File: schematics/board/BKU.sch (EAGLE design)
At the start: 76 parts, among them Q1 8MHz, Q2 32,768KHz, U1 STM32F405RGT6

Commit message: Пытаем плату БКУ компоновкой
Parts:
- removed JP1: (no value), pinhead:PINHD-1X4
- removed LED-G#2: (no value), led:LEDCHIPLED_0603
- removed R10, R11, R14, R4: 10k, resistor:R-US_R0603
- removed R19: 1M, resistor:R-US_R0603
- removed R20: 510k, resistor:R-US_R0603
- removed R28: 2k, resistor:R-US_R0603
- removed U$9: FS8205A+, CanCubeSat:FS8205A+
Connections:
- removed net 3V3: U$4.3V3/BUS
- removed net B1_KVCC: R10.1, R11.1, R19.1, R20.1, U$18.Q0
- removed net BUS-: LED-G#2.A, R20.2, U$9.S1
- removed net GND2: R27.2
- removed net N$1: JP1.4, U1.PA6/SPI1_MISO
- removed net N$10: JP1.3, U1.PA7/SPI1_MOSI
- removed net N$11: R14.1, U1.PA15
- removed net N$12: R4.1, U1.PB3
- removed net N$16: JP1.1, U1.PA4/USART2_CK
- removed net N$2: JP1.2, U1.PA5/SPI1_SCK
- removed net N$50: LED-B#2.A
- removed net N$52: LED-G#2.C, R28.2
- removed net N$8: R10.2, U$9.G1
- removed net N$9: R11.2, U$9.G2
- net 5V: no longer R28.1
- net BUS+: no longer R19.2
- net GND: now also R27.2; no longer U$9.HEAT, U$9.S2
- net N$3: now also LED-B#2.A
- net VDD: now also U$4.3V3/BUS; no longer R14.2, R4.2
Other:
- moved on the sheet: C1, C15, C16, C17, C5, R12

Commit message: Изменения в БКУ
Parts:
- GPS: value GPS -> GPSNEO6M; device CanCubeSat:GPS -> CanCubeSat:GPSNEO6M
- JTAG: device pinheadCS:PINHD-1X4 -> pinheadCS:PINHD-1X6
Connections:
- net GND: now also JTAG.1, U1.BOOT0, U1.PB2/BOOT1, U1.VSS
- net MTCK: now also JTAG.5; no longer JTAG.3
- net MTDI: now also JTAG.6; no longer JTAG.4
- net MTDO: now also JTAG.3; no longer JTAG.1
- net MTMS: now also JTAG.4; no longer JTAG.2
- net VDD: now also JTAG.2
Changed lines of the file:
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@@
 <part name="C10" library="rcl" library_urn="urn:adsk.eagle:library:334" deviceset="C-EU" device="C0603" package3d_urn="urn:adsk.eagle:package:23616/2" value="10pF"/>
 <part name="C11" library="rcl" library_urn="urn:adsk.eagle:library:334" deviceset="C-EU" device="C0603" package3d_urn="urn:adsk.eagle:package:23616/2" value="10pF"/>
-<part name="GPS" library="CanCubeSat" deviceset="GPS" device=""/>
+<part name="GPS" library="CanCubeSat" deviceset="GPS" device="NEO6M" value="GPSNEO6M"/>
 <part name="SUPPLY4" library="supply2" library_urn="urn:adsk.eagle:library:372" deviceset="GND" device=""/>
 <part name="RADIO" library="CanCubeSat" deviceset="RADIO" device=""/>
@@
 <part name="LED1" library="led" library_urn="urn:adsk.eagle:library:259" deviceset="LED" device="CHIPLED_0603" package3d_urn="urn:adsk.eagle:package:15822/2"/>
 <part name="R7" library="resistor" library_urn="urn:adsk.eagle:library:348" deviceset="R-US_" device="R0603" package3d_urn="urn:adsk.eagle:package:23555/3" value="10k"/>
-<part name="JTAG" library="pinheadCS" deviceset="PINHD-1X4" device=""/>
 <part name="MAG" library="pinheadCS" deviceset="PINHD-1X4" device=""/>
 <part name="R15" library="resistor" library_urn="urn:adsk.eagle:library:348" deviceset="R-US_" device="R0603" package3d_urn="urn:adsk.eagle:package:23555/3" value="2k"/>
@@
 <part name="LED-B#2" library="led" library_urn="urn:adsk.eagle:library:259" deviceset="LED" device="CHIPLED_0603" package3d_urn="urn:adsk.eagle:package:15822/2"/>
 <part name="R29" library="resistor" library_urn="urn:adsk.eagle:library:348" deviceset="R-US_" device="R0603" package3d_urn="urn:adsk.eagle:package:23555/3" value="10k"/>
+<part name="JTAG" library="pinheadCS" deviceset="PINHD-1X6" device=""/>
 </parts>
 <sheets>
@@
 <attribute name="VALUE" x="224.282" y="166.37" size="1.778" layer="96" rot="R90"/>
 </instance>
-<instance part="JTAG" gate="A" x="48.26" y="114.3" smashed="yes" rot="R180">
-<attribute name="NAME" x="54.61" y="106.045" size="1.778" layer="95" rot="R180"/>
-<attribute name="VALUE" x="54.61" y="121.92" size="1.778" layer="96" rot="R180"/>
-</instance>
 <instance part="MAG" gate="A" x="-86.36" y="63.5" smashed="yes" rot="R90">
 <attribute name="NAME" x="-94.615" y="57.15" size="1.778" layer="95" rot="R90"/>
@@
 <attribute name="NAME" x="232.41" y="280.8986" size="1.778" layer="95"/>
 <attribute name="VALUE" x="232.41" y="276.098" size="1.778" layer="96"/>
+</instance>
+<instance part="JTAG" gate="A" x="48.26" y="111.76" smashed="yes" rot="R180">
+<attribute name="NAME" x="52.07" y="100.965" size="1.778" layer="95" rot="R180"/>
+<attribute name="VALUE" x="54.61" y="119.38" size="1.778" layer="96" rot="R180"/>
 </instance>
 </instances>
@@
 <label x="248.92" y="279.4" size="1.778" layer="95" rot="R180"/>
 </segment>
+<segment>
+<pinref part="JTAG" gate="A" pin="1"/>
+<wire x1="50.8" y1="104.14" x2="66.04" y2="104.14" width="0.1524" layer="91"/>
+<label x="58.42" y="104.14" size="1.778" layer="95"/>
+</segment>
+<segment>
+<pinref part="U1" gate="G$1" pin="VSS"/>
+<wire x1="292.1" y1="73.66" x2="304.8" y2="73.66" width="0.1524" layer="91"/>
+<label x="299.72" y="73.66" size="1.778" layer="95"/>
+</segment>
+<segment>
+<pinref part="U1" gate="G$1" pin="BOOT0"/>
+<wire x1="231.14" y1="167.64" x2="231.14" y2="180.34" width="0.1524" layer="91"/>
+<label x="231.14" y="175.26" size="1.778" layer="95" rot="R90"/>
+</segment>
+<segment>
+<pinref part="U1" gate="G$1" pin="PB2/BOOT1"/>
+<wire x1="231.14" y1="111.76" x2="218.44" y2="111.76" width="0.1524" layer="91"/>
+<label x="218.44" y="111.76" size="1.778" layer="95"/>
+</segment>
 </net>
 <net name="5V" class="0">
@@
 <label x="-121.92" y="170.18" size="1.778" layer="95"/>
 <pinref part="U$4" gate="G$1" pin="3V3/BUS"/>
+</segment>
+<segment>
+<pinref part="JTAG" gate="A" pin="2"/>
+<wire x1="50.8" y1="106.68" x2="66.04" y2="106.68" width="0.1524" layer="91"/>
+<label x="58.42" y="106.68" size="1.778" layer="95"/>
 </segment>
 </net>
@@
 <net name="MTDI" class="0">
 <segment>
-<pinref part="JTAG" gate="A" pin="4"/>
 <wire x1="50.8" y1="116.84" x2="66.04" y2="116.84" width="0.1524" layer="91"/>
 <label x="58.42" y="116.84" size="1.778" layer="95"/>
+<pinref part="JTAG" gate="A" pin="6"/>
 </segment>
 <segment>
@@
 <net name="MTCK" class="0">
 <segment>
-<pinref part="JTAG" gate="A" pin="3"/>
 <wire x1="50.8" y1="114.3" x2="66.04" y2="114.3" width="0.1524" layer="91"/>
 <label x="58.42" y="114.3" size="1.778" layer="95"/>
+<pinref part="JTAG" gate="A" pin="5"/>
 </segment>
 <segment>
@@
 <net name="MTMS" class="0">
 <segment>
-<pinref part="JTAG" gate="A" pin="2"/>
 <wire x1="50.8" y1="111.76" x2="66.04" y2="111.76" width="0.1524" layer="91"/>
 <label x="58.42" y="111.76" size="1.778" layer="95"/>
+<pinref part="JTAG" gate="A" pin="4"/>
 </segment>
 <segment>
@@
 <net name="MTDO" class="0">
 <segment>
-<pinref part="JTAG" gate="A" pin="1"/>
 <wire x1="50.8" y1="109.22" x2="66.04" y2="109.22" width="0.1524" layer="91"/>
 <label x="58.42" y="109.22" size="1.778" layer="95"/>
-</segment>
-<segment>
+<pinref part="JTAG" gate="A" pin="3"/>
+</segment>
+<segment>

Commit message: Изменения в БКУ
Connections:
- net GND: now also U1.VSSA
- net VDD: now also U1.VDDA
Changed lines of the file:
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@@
 <wire x1="292.1" y1="73.66" x2="304.8" y2="73.66" width="0.1524" layer="91"/>
 <label x="299.72" y="73.66" size="1.778" layer="95"/>
+<pinref part="U1" gate="G$1" pin="VSSA"/>
+<wire x1="292.1" y1="71.12" x2="292.1" y2="73.66" width="0.1524" layer="91"/>
+<junction x="292.1" y="73.66"/>
 </segment>
 <segment>
@@
 <label x="299.72" y="175.26" size="1.778" layer="95"/>
 <pinref part="LED2" gate="G$1" pin="A"/>
-</segment>
-<segment>
+<pinref part="U1" gate="G$1" pin="VDDA"/>
+<wire x1="292.1" y1="172.72" x2="292.1" y2="175.26" width="0.1524" layer="91"/>
+<junction x="292.1" y="175.26"/>
+</segment>
+<segment>

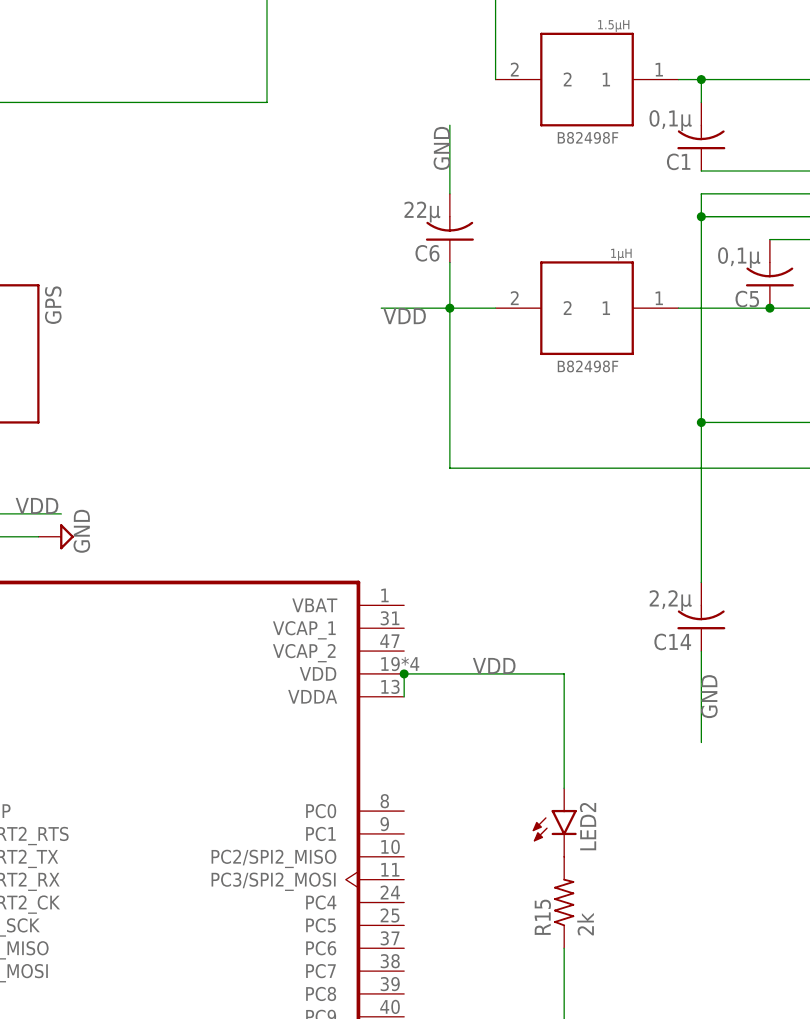
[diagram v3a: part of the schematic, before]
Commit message: Добавлена батарейка в БКУ
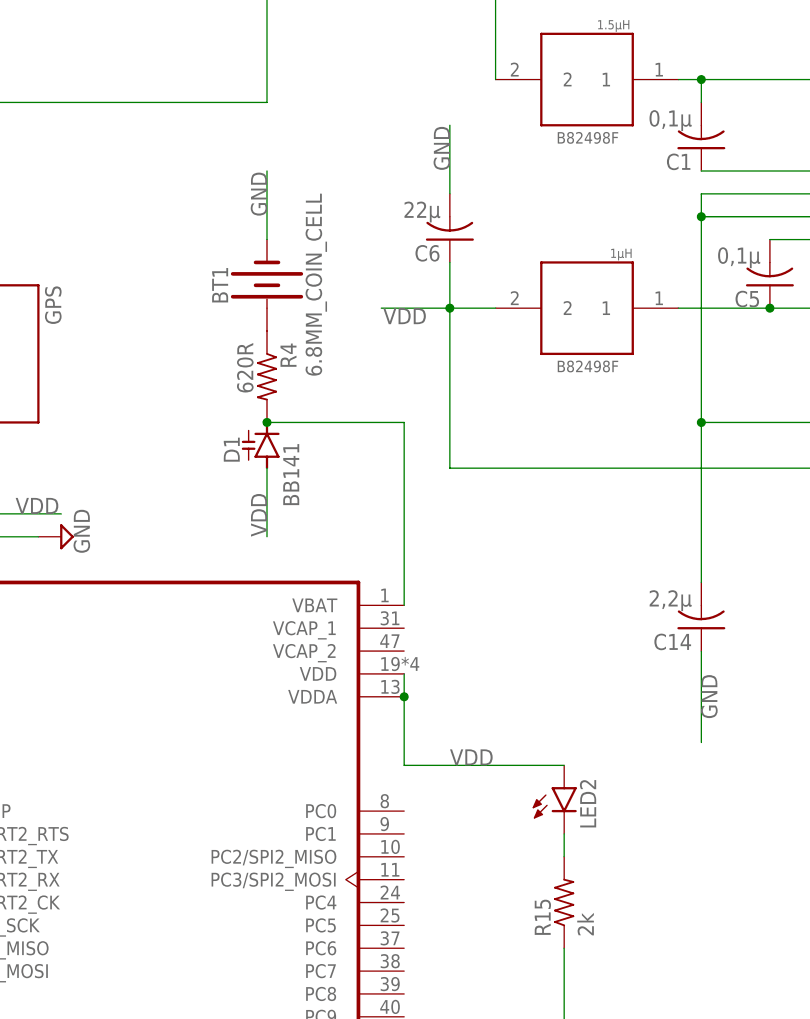
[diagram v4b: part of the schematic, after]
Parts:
- added BT1: 6.8MM_COIN_CELL, SparkFun-Batteries:BATTERY-6.8MM_SMD
- added D1: BB141, diode:BB141
- added R4: 620R, resistor:R-US_R0603
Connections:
- new net N$1: BT1.+, R4.1
- new net N$2: D1.C, R4.2, U1.VBAT
- net GND: now also BT1.-
- net VDD: now also D1.A
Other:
- moved on the sheet: LED2

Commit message: Изменения в БКУ
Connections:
- net 5V: now also RADIO.VCC
- net VDD: no longer RADIO.VCC
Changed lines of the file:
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@@
 <pinref part="BSK4" gate="A" pin="2"/>
+</segment>
+<segment>
+<pinref part="RADIO" gate="G$1" pin="VCC"/>
+<wire x1="220.98" y1="264.16" x2="220.98" y2="271.78" width="0.1524" layer="91"/>
+<label x="220.98" y="266.7" size="1.778" layer="95" rot="R90"/>
 </segment>
 </net>
@@
 </segment>
 <segment>
-<pinref part="RADIO" gate="G$1" pin="VCC"/>
-<wire x1="220.98" y1="264.16" x2="220.98" y2="271.78" width="0.1524" layer="91"/>
-<label x="220.98" y="266.7" size="1.778" layer="95" rot="R90"/>
-</segment>
-<segment>

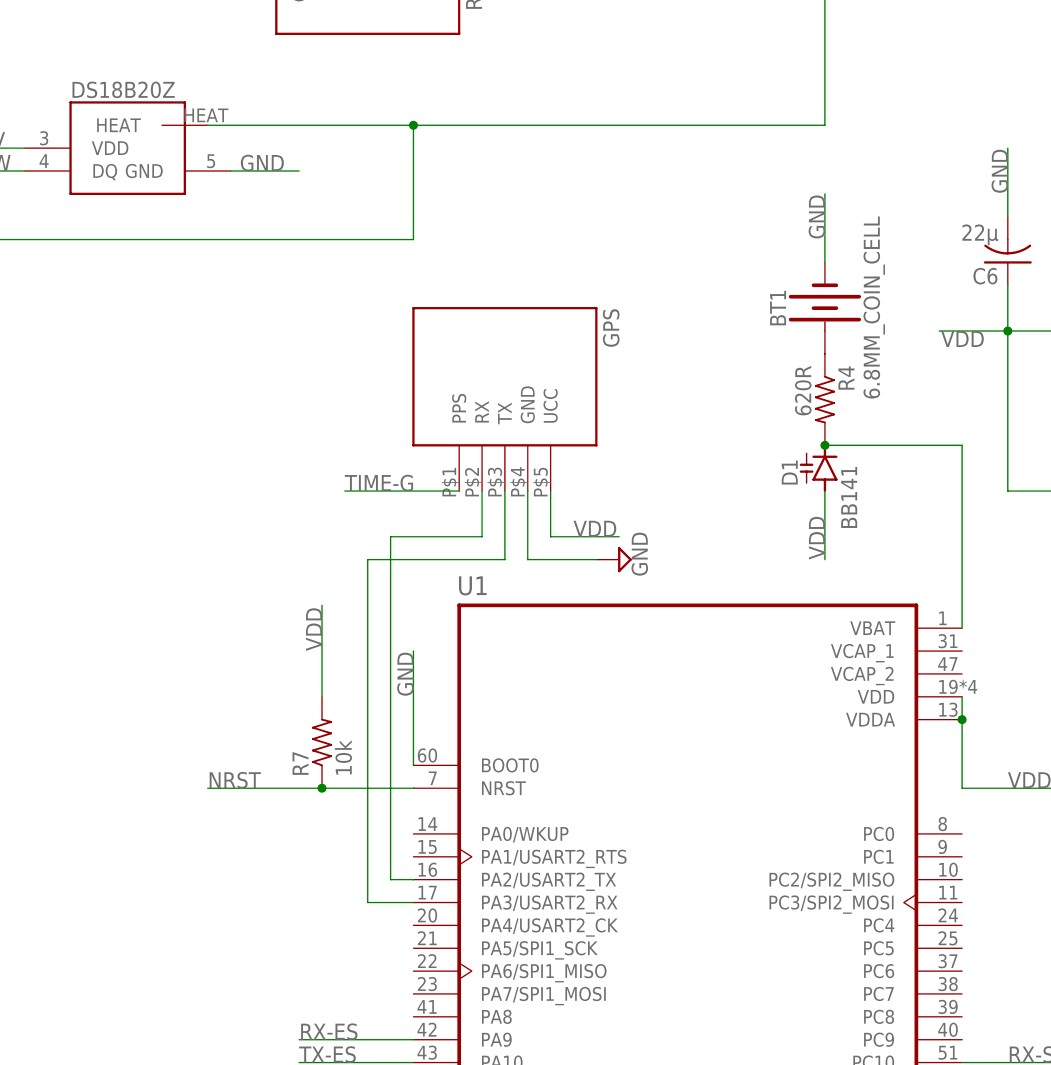
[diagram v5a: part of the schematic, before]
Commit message: Разводка БКУ кроме 1 дорожки к есп (RX-R)
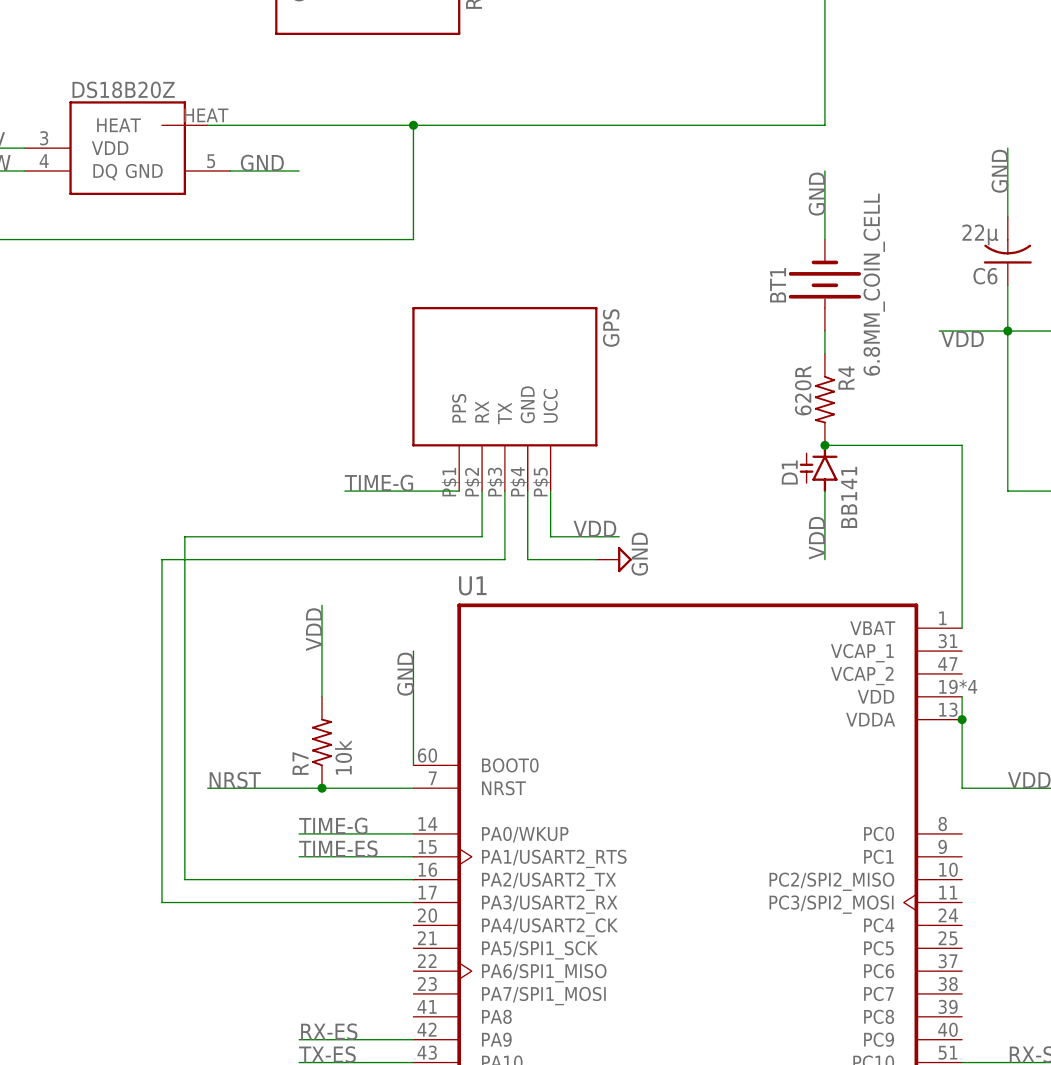
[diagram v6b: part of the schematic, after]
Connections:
- net TIME-ES: now also U1.PA1/USART2_RTS
- net TIME-G: now also U1.PA0/WKUP
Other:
- moved on the sheet: BT1
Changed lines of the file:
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@@
 <attribute name="VALUE" x="273.558" y="212.09" size="1.778" layer="96" rot="R270"/>
 </instance>
-<instance part="BT1" gate="G$1" x="276.86" y="218.44" smashed="yes" rot="R90">
-<attribute name="NAME" x="272.542" y="218.44" size="1.778" layer="95" font="vector" rot="R90" align="bottom-center"/>
-<attribute name="VALUE" x="281.178" y="218.44" size="1.778" layer="96" font="vector" rot="R90" align="top-center"/>
+<instance part="BT1" gate="G$1" x="276.86" y="220.98" smashed="yes" rot="R90">
+<attribute name="NAME" x="272.542" y="220.98" size="1.778" layer="95" font="vector" rot="R90" align="bottom-center"/>
+<attribute name="VALUE" x="281.178" y="220.98" size="1.778" layer="96" font="vector" rot="R90" align="top-center"/>
 </instance>
 </instances>
@@
 <segment>
 <pinref part="BT1" gate="G$1" pin="-"/>
-<wire x1="276.86" y1="223.52" x2="276.86" y2="231.14" width="0.1524" layer="91"/>
-<label x="276.86" y="226.06" size="1.778" layer="95" rot="R90"/>
+<wire x1="276.86" y1="226.06" x2="276.86" y2="233.68" width="0.1524" layer="91"/>
+<label x="276.86" y="228.6" size="1.778" layer="95" rot="R90"/>
 </segment>
 </net>
@@
 <segment>
 <pinref part="U1" gate="G$1" pin="PA2/USART2_TX"/>
-<wire x1="231.14" y1="154.94" x2="228.6" y2="154.94" width="0.1524" layer="91"/>
-<wire x1="228.6" y1="154.94" x2="228.6" y2="193.04" width="0.1524" layer="91"/>
+<wire x1="231.14" y1="154.94" x2="205.74" y2="154.94" width="0.1524" layer="91"/>
+<wire x1="205.74" y1="154.94" x2="205.74" y2="193.04" width="0.1524" layer="91"/>
 <pinref part="GPS" gate="G$1" pin="RX"/>
 <wire x1="238.76" y1="198.12" x2="238.76" y2="193.04" width="0.1524" layer="91"/>
-<wire x1="238.76" y1="193.04" x2="228.6" y2="193.04" width="0.1524" layer="91"/>
+<wire x1="238.76" y1="193.04" x2="205.74" y2="193.04" width="0.1524" layer="91"/>
 </segment>
 </net>
@@
 <segment>
 <pinref part="U1" gate="G$1" pin="PA3/USART2_RX"/>
-<wire x1="231.14" y1="152.4" x2="226.06" y2="152.4" width="0.1524" layer="91"/>
-<wire x1="241.3" y1="190.5" x2="226.06" y2="190.5" width="0.1524" layer="91"/>
-<wire x1="226.06" y1="190.5" x2="226.06" y2="152.4" width="0.1524" layer="91"/>
+<wire x1="231.14" y1="152.4" x2="203.2" y2="152.4" width="0.1524" layer="91"/>
+<wire x1="241.3" y1="190.5" x2="203.2" y2="190.5" width="0.1524" layer="91"/>
+<wire x1="203.2" y1="190.5" x2="203.2" y2="152.4" width="0.1524" layer="91"/>
 <pinref part="GPS" gate="G$1" pin="TX"/>
 <wire x1="241.3" y1="190.5" x2="241.3" y2="198.12" width="0.1524" layer="91"/>
@@
 <label x="223.52" y="198.12" size="1.778" layer="95"/>
 </segment>
+<segment>
+<pinref part="U1" gate="G$1" pin="PA0/WKUP"/>
+<wire x1="231.14" y1="160.02" x2="218.44" y2="160.02" width="0.1524" layer="91"/>
+<label x="218.44" y="160.02" size="1.778" layer="95"/>
+</segment>
 </net>
 <net name="TIME-ES" class="0">
@@
 <wire x1="83.82" y1="45.72" x2="91.44" y2="45.72" width="0.1524" layer="91"/>
 <label x="86.36" y="45.72" size="1.778" layer="95"/>
+</segment>
+<segment>
+<pinref part="U1" gate="G$1" pin="PA1/USART2_RTS"/>
+<wire x1="231.14" y1="157.48" x2="218.44" y2="157.48" width="0.1524" layer="91"/>
+<label x="218.44" y="157.48" size="1.778" layer="95"/>
 </segment>
 </net>
@@
 <pinref part="R4" gate="G$1" pin="1"/>
 <pinref part="BT1" gate="G$1" pin="+"/>
-</segment>
-</net>
+<wire x1="276.86" y1="215.9" x2="276.86" y2="213.36" width="0.1524" layer="91"/>
+</segment>
+</net>
